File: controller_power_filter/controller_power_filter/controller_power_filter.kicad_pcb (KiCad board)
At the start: 2 copper layers, 95 x 35 mm, 22 parts, among them J1 Screw_Terminal_01x03, J2 Screw_Terminal_01x03

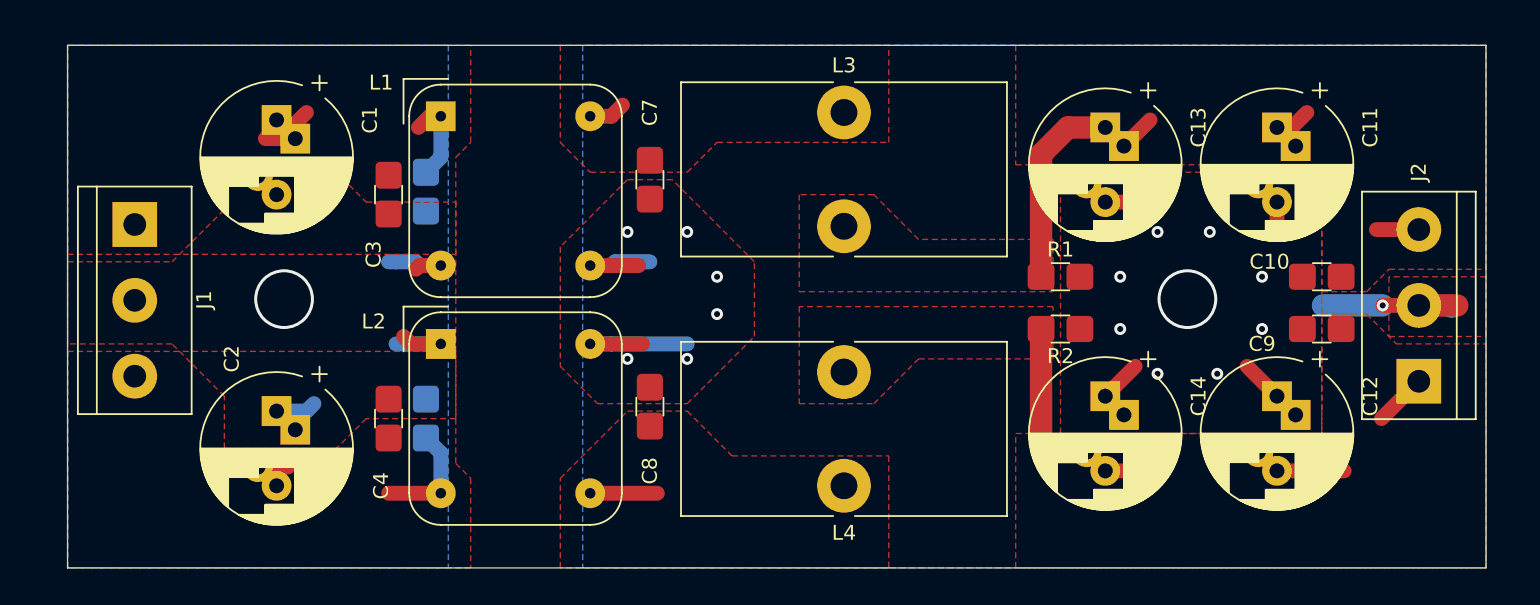
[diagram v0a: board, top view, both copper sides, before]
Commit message: minor footprint adjustment to the choke/filter board
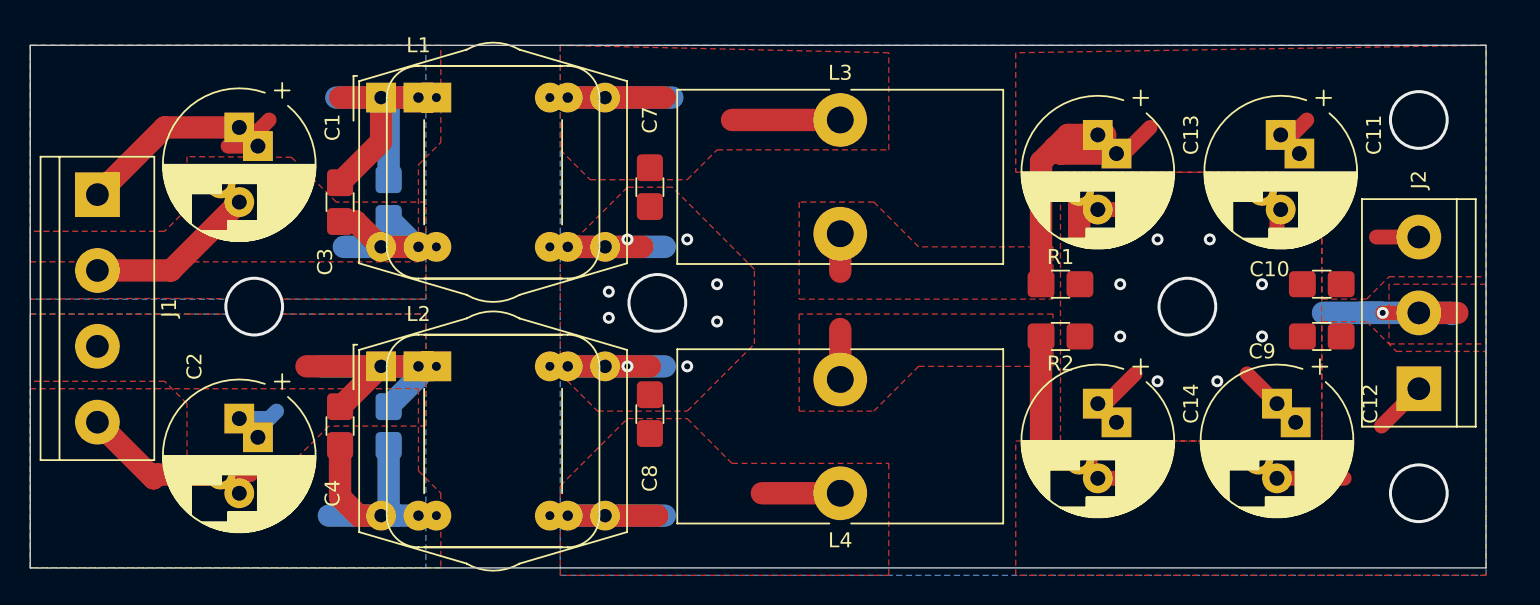
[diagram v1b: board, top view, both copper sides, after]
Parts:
- J1: value Screw_Terminal_01x03 -> Screw_Terminal_01x04; footprint TerminalBlock:TerminalBlock_bornier-3_P5.08mm -> TerminalBlock:TerminalBlock_bornier-4_P5.08mm
- L1: value L_Core_Ferrite_Coupled -> RN112; footprint Inductor_THT:Choke_Schaffner_RN102-04-14.0x14.0mm -> SamacSys_Parts:Choke_Schaffner_RN102_112_204
- L2: value Inductor_THT:Choke_Schaffner_RN102-04-14.0x14.0mm -> RN112; footprint Inductor_THT:Choke_Schaffner_RN102-04-14.0x14.0mm -> SamacSys_Parts:Choke_Schaffner_RN102_112_204
- moved C3 3.29 mm to (113.2, 125.5)
- moved C4 3.29 mm to (113.2, 140.5)
- moved J1 3.20 mm to (97.0, 125.0)
- moved C1 2.55 mm to (106.5, 120.5)
- moved C2 2.55 mm to (106.5, 140.0)
- moved C5 2.55 mm to (116.5, 125.3)
- moved C6 2.55 mm to (116.5, 140.5)
- moved L2 2.12 mm to (118.5, 136.5)
- moved L1 1.95 mm to (118.5, 118.5)
- moved C13 0.71 mm to (164.0, 121.0)
- moved C14 0.71 mm to (164.0, 139.0)
- moved C11 0.56 mm to (176.2, 121.0)
- moved L3 0.56 mm to (146.8, 120.0)
- moved L4 0.56 mm to (146.8, 145.0)
- moved C10 0.50 mm to (179.0, 134.5)
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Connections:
- C1 pad 2: /GND_P -> Net-(C1-Pad2)
- C2 pad 1: /GND_P -> Net-(C2-Pad1)
- C3 pad 2: /GND_P -> Net-(C1-Pad2)
- C4 pad 1: /GND_P -> Net-(C2-Pad1)
- C5 pad 2: /GND_P -> Net-(C1-Pad2)
- C6 pad 1: /GND_P -> Net-(C2-Pad1)
- J1 pad 2: /GND_P -> Net-(C1-Pad2)
- J1 pad 3: /-VP -> Net-(C2-Pad1)
- L1 pad 3: /GND_P -> Net-(C1-Pad2)
- L2 pad 1: /GND_P -> Net-(C2-Pad1)
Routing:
- net /+VP: track 10.0 -> 41.1 mm
- net Net-(C2-Pad1): track 0.00 -> 26.5 mm
- net Net-(C1-Pad2): track 0.00 -> 25.0 mm
- net /-VP: track 11.6 -> 32.7 mm
- net /+VL: track 2.47 -> 23.2 mm
- net /GND_A: track 39.2 -> 57.0 mm, vias 15 -> 18
- net /-VL: track 4.50 -> 20.2 mm
- net /GND_P: track 13.8 -> 0.00 mm, vias 1 -> 0
- net /+VA: track 21.0 -> 27.8 mm
- net /-VA: track 25.0 -> 28.4 mm
- net (no net): vias 1 -> 4
- added copper zone on B.Cu, net Net-(C1-Pad2)
- added copper zone on F.Cu, net Net-(C1-Pad2)
- added copper zone on B.Cu, net Net-(C2-Pad1)
- added copper zone on F.Cu, net Net-(C2-Pad1)
- removed copper zone on B.Cu, net /GND_P
- removed copper zone on F.Cu, net /GND_P
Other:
- board size 95 x 35 mm -> 97.5 x 35 mm

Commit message: Relay array board; Last checkup; Gerberfile updates
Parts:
- added J3: Conn_Coaxial, Connector_Coaxial:U.FL_Hirose_U.FL-R-SMT-1_Vertical, B.Cu at (181.8, 125.2)
- added J4: Conn_Coaxial, Connector_Coaxial:U.FL_Hirose_U.FL-R-SMT-1_Vertical, B.Cu at (181.8, 140.2)
- added L5: 2124-V-RC, Inductor_SMD:L_10.4x10.4_H4.8, F.Cu at (146.8, 123.8)
- added L6: 2124-V-RC, Inductor_SMD:L_10.4x10.4_H4.8, F.Cu at (146.8, 141.2)
- J2: value Screw_Terminal_01x03 -> Screw_Terminal_01x04; footprint TerminalBlock:TerminalBlock_bornier-3_P5.08mm -> TerminalBlock:TerminalBlock_bornier-4_P5.08mm
- moved J2 13.1 mm to (185.8, 124.9), turned to 270 degrees
- moved C9 0.50 mm to (179.0, 130.5)
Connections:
- C10 pad 1: /GND_A -> Net-(C10-Pad1)
- C11 pad 2: /GND_A -> Net-(C11-Pad2)
- C12 pad 1: /GND_A -> Net-(C10-Pad1)
- C13 pad 2: /GND_A -> Net-(C11-Pad2)
- C14 pad 1: /GND_A -> Net-(C10-Pad1)
- C7 pad 2: /GND_A -> Net-(C11-Pad2)
- C8 pad 1: /GND_A -> Net-(C10-Pad1)
- C9 pad 2: /GND_A -> Net-(C11-Pad2)
- J2 pad 1: /-VA -> /+VA
- J2 pad 2: /GND_A -> Net-(C11-Pad2)
- J2 pad 3: /+VA -> Net-(C10-Pad1)
- L1 pad 4: /GND_A -> Net-(C11-Pad2)
- L2 pad 2: /GND_A -> Net-(C10-Pad1)
- R1 pad 2: /GND_A -> Net-(C11-Pad2)
- R2 pad 1: /GND_A -> Net-(C10-Pad1)
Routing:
- net /GND_A: track 57.0 -> 0.00 mm, vias 18 -> 0
- net Net-(C11-Pad2): track 0.00 -> 47.7 mm, vias 0 -> 7
- net Net-(C10-Pad1): track 0.00 -> 43.5 mm, vias 0 -> 7
- net /-VA: track 28.4 -> 55.5 mm
- net /+VA: track 27.8 -> 51.0 mm
- net /+VL: track 23.2 -> 32.3 mm
- net /-VL: track 20.2 -> 26.0 mm
- net (no net): vias 4 -> 3
- added copper zone on B.Cu, net Net-(C10-Pad1)
- added copper zone on F.Cu, net Net-(C10-Pad1)
- added copper zone on B.Cu, net Net-(C11-Pad2)
- added copper zone on F.Cu, net Net-(C11-Pad2)
- removed copper zone on B.Cu, net /GND_A
- removed copper zone on F.Cu, net /GND_A
